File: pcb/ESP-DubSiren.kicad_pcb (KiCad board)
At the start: 2 copper layers, 98 x 72 mm, 13 parts, among them SW1 TRIGGER, SW2 MOD DOWN, SW3 MOD UP, SW4 ECHO CUT, U1 ESP32-S3-DevKitC-1 N16R8, U2 PCM5102A BREAKOUT PROVISIONAL

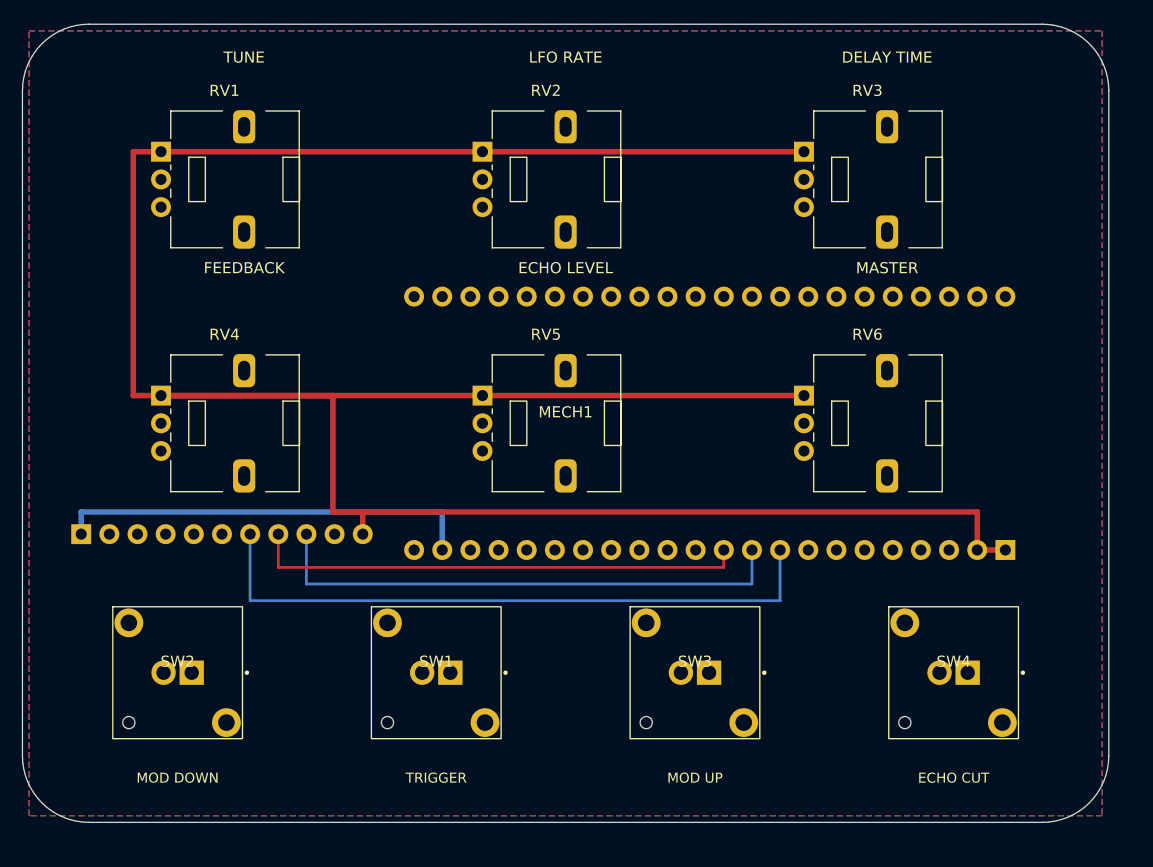
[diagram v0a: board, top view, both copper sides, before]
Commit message: pcb: add ESP32-S3 mainboard V1 preproduction design
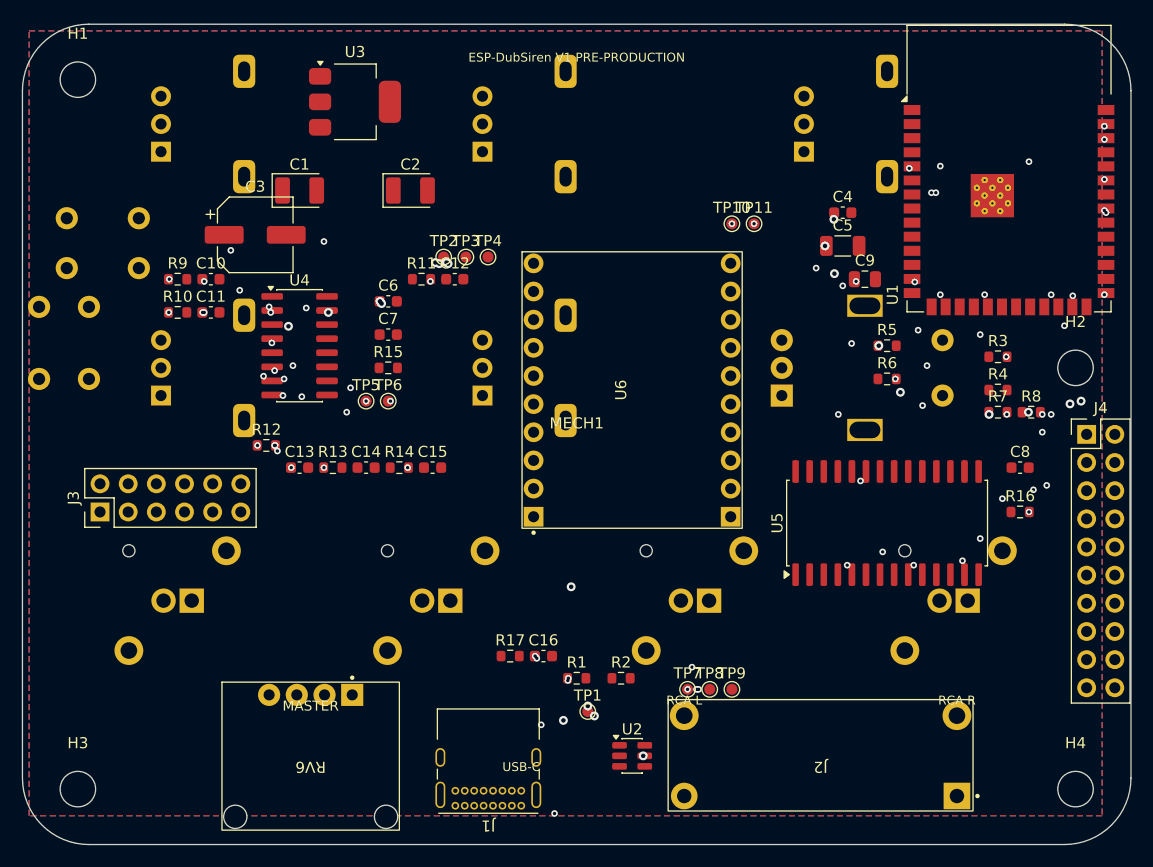
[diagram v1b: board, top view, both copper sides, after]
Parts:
- added C1: 10uF 10V tantalum IN, Capacitor_Tantalum_SMD:CP_EIA-3528-21_Kemet-B, F.Cu at (25.0, 15.0)
- added C10: 100nF POT1, Capacitor_SMD:C_0603_1608Metric, F.Cu at (17.0, 23.0)
- added C11: 100nF POT2, Capacitor_SMD:C_0603_1608Metric, F.Cu at (17.0, 26.0)
- added C12: 100nF POT3, Capacitor_SMD:C_0603_1608Metric, F.Cu at (39.0, 23.0)
- added C13: 100nF POT4, Capacitor_SMD:C_0603_1608Metric, F.Cu at (25.0, 40.0)
- added C14: 100nF POT5, Capacitor_SMD:C_0603_1608Metric, F.Cu at (31.0, 40.0)
- added C15: 100nF MASTER, Capacitor_SMD:C_0603_1608Metric, F.Cu at (37.0, 40.0)
- added C16: 1nF DNP CHASSIS-GND, Capacitor_SMD:C_0603_1608Metric, F.Cu at (47.0, 57.0)
- added C2: 10uF 10V tantalum OUT, Capacitor_Tantalum_SMD:CP_EIA-3528-21_Kemet-B, F.Cu at (35.0, 15.0)
- added C3: 47uF 10V +5V bulk, Capacitor_SMD:CP_Elec_6.3x5.3, F.Cu at (21.0, 19.0)
- added C4: 100nF ESP32, Capacitor_SMD:C_0603_1608Metric, F.Cu at (74.0, 17.0)
- added C5: 10uF ESP32, Capacitor_SMD:C_1206_3216Metric, F.Cu at (74.0, 20.0)
- added C6: 100nF MCP3208 VDD, Capacitor_SMD:C_0603_1608Metric, F.Cu at (33.0, 25.0)
- added C7: 100nF MCP3208 VREF, Capacitor_SMD:C_0603_1608Metric, F.Cu at (33.0, 28.0)
- added C8: 100nF MCP23017, Capacitor_SMD:C_0603_1608Metric, F.Cu at (90.0, 40.0)
- added C9: 1uF EN RC, Capacitor_SMD:C_0805_2012Metric, F.Cu at (76.0, 23.0)
- added H1: MountingHole_3.2mm_M3, MountingHole:MountingHole_3.2mm_M3, F.Cu at (5.00, 5.00)
- added H2: MountingHole_3.2mm_M3, MountingHole:MountingHole_3.2mm_M3, F.Cu at (95.0, 31.0)
- added H3: MountingHole_3.2mm_M3, MountingHole:MountingHole_3.2mm_M3, F.Cu at (5.00, 69.0)
- added H4: MountingHole_3.2mm_M3, MountingHole:MountingHole_3.2mm_M3, F.Cu at (95.0, 69.0)
- added J1: USB-C USB2.0 DEVICE, Connector_USB:USB_C_Receptacle_GCT_USB4085, F.Cu at (45.0, 70.5)
- added J2: AUDIO OUT L/R, ESP-DubSiren:Switchcraft_PJRAS2X1S02X, F.Cu at (72.0, 66.0)
- added J3: J_DISPLAY, Connector_PinHeader_2.54mm:PinHeader_2x06_P2.54mm_Vertical, F.Cu at (7.00, 44.0)
- added J4: J_EXP, Connector_PinHeader_2.54mm:PinHeader_2x10_P2.54mm_Vertical, F.Cu at (96.0, 37.0)
- added R1: 5.1k CC1, Resistor_SMD:R_0603_1608Metric, F.Cu at (50.0, 59.0)
- added R10: 1k POT2, Resistor_SMD:R_0603_1608Metric, F.Cu at (14.0, 26.0)
- added R11: 1k POT3, Resistor_SMD:R_0603_1608Metric, F.Cu at (36.0, 23.0)
- added R12: 1k POT4, Resistor_SMD:R_0603_1608Metric, F.Cu at (22.0, 38.0)
- added R13: 1k POT5, Resistor_SMD:R_0603_1608Metric, F.Cu at (28.0, 40.0)
- added R14: 1k MASTER, Resistor_SMD:R_0603_1608Metric, F.Cu at (34.0, 40.0)
- added R15: 10k ADC CS pull-up, Resistor_SMD:R_0603_1608Metric, F.Cu at (33.0, 31.0)
- added R16: 10k IOEXP RESET pull-up, Resistor_SMD:R_0603_1608Metric, F.Cu at (90.0, 44.0)
- added R17: 0R DNP CHASSIS-GND, Resistor_SMD:R_0603_1608Metric, F.Cu at (44.0, 57.0)
- added R2: 5.1k CC2, Resistor_SMD:R_0603_1608Metric, F.Cu at (54.0, 59.0)
- added R3: 22R USB D-, Resistor_SMD:R_0603_1608Metric, F.Cu at (88.0, 30.0)
- added R4: 22R USB D+, Resistor_SMD:R_0603_1608Metric, F.Cu at (88.0, 33.0)
- added R5: 10k EN pull-up, Resistor_SMD:R_0603_1608Metric, F.Cu at (78.0, 29.0)
- added R6: 10k BOOT pull-up, Resistor_SMD:R_0603_1608Metric, F.Cu at (78.0, 32.0)
- added R7: 4.7k I2C SDA, Resistor_SMD:R_0603_1608Metric, F.Cu at (88.0, 35.0)
- added R8: 4.7k I2C SCL, Resistor_SMD:R_0603_1608Metric, F.Cu at (91.0, 35.0)
- added R9: 1k POT1, Resistor_SMD:R_0603_1608Metric, F.Cu at (14.0, 23.0)
- added SW5: RESET B3F-1000, Button_Switch_THT:SW_PUSH_6mm_H4.3mm, B.Cu at (4.00, 22.0)
- added SW6: BOOT B3F-1000, Button_Switch_THT:SW_PUSH_6mm_H4.3mm, B.Cu at (6.00, 32.0)
- added SW7: ENCODER EC11E09244AQ, Rotary_Encoder:RotaryEncoder_Alps_EC11E-Switch_Vertical_H20mm, B.Cu at (68.5, 33.5)
- added TP1: +5V TEST, TestPoint:TestPoint_Pad_D1.0mm, F.Cu at (51.0, 62.0)
- added TP10: UART RX TEST, TestPoint:TestPoint_Pad_D1.0mm, F.Cu at (64.0, 18.0)
- added TP11: UART TX TEST, TestPoint:TestPoint_Pad_D1.0mm, F.Cu at (66.0, 18.0)
- added TP2: +3V3 TEST, TestPoint:TestPoint_Pad_D1.0mm, F.Cu at (38.0, 21.0)
- added TP3: GND TEST, TestPoint:TestPoint_Pad_D1.0mm, F.Cu at (40.0, 21.0)
- added TP4: GND TEST, TestPoint:TestPoint_Pad_D1.0mm, F.Cu at (42.0, 21.0)
- added TP5: ADC CH6 TEST, TestPoint:TestPoint_Pad_D1.0mm, F.Cu at (31.0, 34.0)
- added TP6: ADC CH7 TEST, TestPoint:TestPoint_Pad_D1.0mm, F.Cu at (33.0, 34.0)
- added TP7: AUDIO L TEST, TestPoint:TestPoint_Pad_D1.0mm, F.Cu at (60.0, 60.0)
- added TP8: AUDIO R TEST, TestPoint:TestPoint_Pad_D1.0mm, F.Cu at (62.0, 60.0)
- added TP9: AUDIO GND TEST, TestPoint:TestPoint_Pad_D1.0mm, F.Cu at (64.0, 60.0)
- added U3: LD1117S33TR, Package_TO_SOT_SMD:SOT-223-3_TabPin2, F.Cu at (30.0, 7.00)
- added U4: MCP3208-CI/SL, Package_SO:SOIC-16_3.9x9.9mm_P1.27mm, F.Cu at (25.0, 29.0)
- added U5: MCP23017-E/SO, Package_SO:SOIC-28W_7.5x17.9mm_P1.27mm, F.Cu at (78.0, 45.0)
- added U6: Adafruit 6421 PCM5122 I2S DAC, ESP-DubSiren:Adafruit_PCM5122_6421, F.Cu at (55.0, 33.0)
- RV1: value TUNE 10k B -> TUNE RK09L 10k B; moved to B.Cu
- RV2: value LFO RATE 10k B -> LFO RATE RK09L 10k B; moved to B.Cu
- RV3: value DELAY TIME 10k B -> DELAY TIME RK09L 10k B; moved to B.Cu
- RV4: value FEEDBACK 10k B -> FEEDBACK RK09L 10k B; moved to B.Cu
- RV5: value ECHO LEVEL 10k B -> ECHO LEVEL RK09L 10k B; moved to B.Cu
- RV6: value MASTER 10k B -> MASTER PTV111-3415A-B103; footprint Potentiometer_THT:Potentiometer_Alps_RK09L_Single_Vertical -> ESP-DubSiren:Bourns_PTV111-3415A-B103
- SW1: value TRIGGER -> TRIGGER PB300STQ; moved to B.Cu
- SW2: value MOD DOWN -> MOD DOWN PB300STQ; moved to B.Cu
- SW3: value MOD UP -> MOD UP PB300STQ; moved to B.Cu
- SW4: value ECHO CUT -> ECHO CUT PB300STQ; moved to B.Cu
- U1: value ESP32-S3-DevKitC-1 N16R8 -> ESP32-S3-WROOM-1-N16R8; footprint ESP-DubSiren:ESP32-S3-DevKitC-1_N16R8 -> RF_Module:ESP32-S3-WROOM-1; moved to F.Cu
- U2: value PCM5102A BREAKOUT PROVISIONAL -> USBLC6-2SC6; footprint ESP-DubSiren:PCM5102A_BREAKOUT_PROVISIONAL -> Package_TO_SOT_SMD:SOT-23-6; moved to F.Cu
- moved RV6 55.1 mm to (26.0, 66.0), turned to 180 degrees
- moved U2 47.6 mm to (55.0, 66.0)
- moved U1 35.5 mm to (89.0, 13.0), turned to 0 degrees
- moved SW1 24.2 mm to (14.0, 52.0)
- moved SW2 24.2 mm to (37.3, 52.0)
- moved SW3 6.50 mm to (60.7, 52.0)
- moved SW4 6.50 mm to (84.0, 52.0)
- moved MECH1 1.41 mm to (50.0, 37.0)
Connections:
- RV1 pad 1: +3V3 -> GND
- RV1 pad 2: /POT_TUNE -> /POT1_RAW
- RV1 pad 3: GND -> +3V3
- RV2 pad 1: +3V3 -> GND
- RV2 pad 2: /POT_LFO_RATE -> /POT2_RAW
- RV2 pad 3: GND -> +3V3
- RV3 pad 1: +3V3 -> GND
- RV3 pad 2: /POT_DELAY -> /POT3_RAW
- RV3 pad 3: GND -> +3V3
- RV4 pad 1: +3V3 -> GND
- RV4 pad 2: /POT_FEEDBACK -> /POT4_RAW
- RV4 pad 3: GND -> +3V3
- RV5 pad 1: +3V3 -> GND
- RV5 pad 2: /POT_ECHO_LEVEL -> /POT5_RAW
- RV5 pad 3: GND -> +3V3
- RV6 pad 1: +3V3 -> GND
- RV6 pad 2: /POT_MASTER -> /MASTER_RAW
- RV6 pad 3: GND -> +3V3
- U1 pad 1: +3V3 -> GND
- U1 pad 12: unconnected-(U1-GPIO8-Pad12) -> /DISPLAY_DC
- U1 pad 13: unconnected-(U1-GPIO3-Pad13) -> /USB_DM
- U1 pad 14: unconnected-(U1-GPIO46-Pad14) -> /USB_DP
- U1 pad 17: unconnected-(U1-GPIO11-Pad17) -> /DISPLAY_CS
- U1 pad 18: unconnected-(U1-GPIO12-Pad18) -> /ADC_CS
- U1 pad 19: unconnected-(U1-GPIO13-Pad19) -> /SPI_MOSI
- U1 pad 20: unconnected-(U1-GPIO14-Pad20) -> /SPI_SCK
- U1 pad 21: +5V -> /SPI_MISO
- U1 pad 22: GND -> /DISPLAY_BL_PWM
- U1 pad 23: GND -> unconnected-(U1-IO21-Pad23)
- U1 pad 24: unconnected-(U1-TX_GPIO43-Pad24) -> /GPIO47
- U1 pad 25: unconnected-(U1-RX_GPIO44-Pad25) -> /GPIO48
- U1 pad 27: unconnected-(U1-GPIO2-Pad27) -> /BOOT_GPIO0
- U1 pad 3: unconnected-(U1-RST-Pad3) -> /ESP_EN
- U1 pad 31: unconnected-(U1-GPIO39-Pad31) -> /GPIO38
- U1 pad 32: unconnected-(U1-GPIO38-Pad32) -> /GPIO39
- U1 pad 33: unconnected-(U1-GPIO37-Pad33) -> /GPIO40
- U1 pad 34: unconnected-(U1-GPIO36-Pad34) -> /GPIO41
- U1 pad 35: unconnected-(U1-GPIO35-Pad35) -> /GPIO42
- U1 pad 36: unconnected-(U1-GPIO0-Pad36) -> /UART_RX
- U1 pad 37: unconnected-(U1-GPIO45-Pad37) -> /UART_TX
- U1 pad 38: unconnected-(U1-GPIO48-Pad38) -> /ENC_B
- U1 pad 39: unconnected-(U1-GPIO47-Pad39) -> /ENC_A
- U1 pad 4: unconnected-(U1-GPIO4-Pad4) -> /IOEXP_INTA
- U1 pad 40: unconnected-(U1-GPIO21-Pad40) -> GND
- U1 pad 41: unconnected-(U1-GPIO20-Pad41) -> GND
- U1 pad 5: unconnected-(U1-GPIO5-Pad5) -> /I2C_SDA
- U1 pad 6: unconnected-(U1-GPIO6-Pad6) -> /I2C_SCL
- U1 pad 7: unconnected-(U1-GPIO7-Pad7) -> /DISPLAY_RST
- U1 pad 8: unconnected-(U1-GPIO15-Pad8) -> /GPIO15
- U2 pad 1: +5V -> /USB_DM_CONN
- U2 pad 2: unconnected-(U2-3V3-Pad2) -> GND
- U2 pad 3: GND -> /USB_DP_CONN
- U2 pad 4: GND -> /USB_DP_ESD
- U2 pad 5: GND -> +5V
- U2 pad 6: GND -> /USB_DM_ESD
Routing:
- net +3V3: track 235.1 -> 0.00 mm, vias 0 -> 17
- net /I2S_BCLK: track 58.4 -> 0.00 mm
- net /I2S_LRCK: track 47.8 -> 0.00 mm
- net /I2S_DATA: track 44.8 -> 0.00 mm
- net +5V: track 38.0 -> 0.00 mm, vias 0 -> 4
- net unconnected-(U5-GPB4-Pad5): vias 0 -> 1
- net /USB_DP: vias 0 -> 1
- net /USB_DM_ESD: vias 0 -> 1
- net /USB_DM: vias 0 -> 3
- net /USB_CC2: vias 0 -> 1
- net /USB_CC1: vias 0 -> 3
- net /UART_TX: vias 0 -> 2
- net /UART_RX: vias 0 -> 2
- net /POT5_RAW: vias 0 -> 1
- net /POT4_RAW: vias 0 -> 1
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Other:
- board size 98 x 72 mm -> 100 x 74 mm
- board text added: "BOOT"
- board text added: "BTN1"
- board text added: "BTN2"
- board text added: "BTN3"
- board text added: "BTN4"
- board text added: "DISPLAY 0.96in KEEP-OUT 27.5 x 27.5 mm (J3)"
- board text added: "DISPLAY J3"
- board text added: "ENC1"
- board text added: "ESP-DubSiren V1 PRE-PRODUCTION"
- board text added: "POT1"
- board text added: "POT2"
- board text added: "POT3"
- board text added: "POT4"
- board text added: "POT5"
- board text added: "RCA L"
- board text added: "RCA R"
- board text added: "RESET"
- board text added: "USB-C"
- board text removed: "DELAY TIME"
- board text removed: "ECHO CUT"
- board text removed: "ECHO LEVEL"
- board text removed: "FEEDBACK"
- board text removed: "LFO RATE"
- board text removed: "MOD DOWN"
- board text removed: "MOD UP"
- board text removed: "TRIGGER"
- board text removed: "TUNE"
